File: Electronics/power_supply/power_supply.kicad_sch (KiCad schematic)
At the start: 83 parts, among them IC1 TLV76033DBZR, IC2 LM5069MMX-2_NOPB, J1 Conn_01x02_Male, J10 9801-0-15-15-23-27-10-0, J12 9801-0-15-15-23-27-10-0, J13 9801-0-15-15-23-27-10-0, J14 9801-0-15-15-23-27-10-0, J2 9801-0-15-15-23-27-10-0, J3 Conn_01x02_Male, J4 821-22-002-10-001101, J5 9801-0-15-15-23-27-10-0, J6 Conn_01x04_Male, J7 Conn_01x02_Male, J8 Conn_01x02_Male, J9 Conn_01x02_Pin, Q1 IPD90N04S4L04ATMA1, Q3 BC857, U1 R-78B5.0-2.0, U2 INA226, U3 INA226

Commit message: PCB fixup
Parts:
- added C30: 0.1uF 50V, Capacitor_SMD:C_0402_1005Metric_Pad0.74x0.62mm_HandSolder, symbol Device:C
- Q3: value BC857 -> MMBT5401; Mouser 583-C857 -> 165-8634
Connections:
- net at IC2.1 (SENSE), R8.1: now also C30.1
- net at IC2.2 (VIN), IC2.3 (UVLO), R8.4: now also C30.2
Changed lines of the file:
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@@
 	)
 	(junction
+		(at 158.75 219.71)
+		(diameter 0)
+		(color 0 0 0 0)
+	)
+	(junction
 		(at 254 246.38)
 		(diameter 0)
@@
 	)
 	(junction
+		(at 162.56 210.82)
+		(diameter 0)
+		(color 0 0 0 0)
+	)
+	(junction
 		(at 351.79 45.72)
 		(diameter 0)
@@
 	(wire
 		(pts
-			(xy 142.24 219.71) (xy 160.02 219.71)
+			(xy 142.24 219.71) (xy 158.75 219.71)
 		)
 		(stroke
@@
 	(wire
 		(pts
-			(xy 162.56 208.28) (xy 162.56 217.17)
+			(xy 162.56 208.28) (xy 162.56 210.82)
 		)
 		(stroke
@@
 	(wire
 		(pts
+			(xy 162.56 210.82) (xy 162.56 217.17)
+		)
+		(stroke
+			(width 0)
+			(type default)
+		)
+	)
+	(wire
+		(pts
 			(xy 341.63 203.2) (xy 346.71 203.2)
 		)
@@
 	(wire
 		(pts
+			(xy 158.75 219.71) (xy 160.02 219.71)
+		)
+		(stroke
+			(width 0)
+			(type default)
+		)
+	)
+	(wire
+		(pts
 			(xy 294.64 95.25) (xy 297.18 95.25)
 		)
@@
 	(wire
 		(pts
+			(xy 158.75 218.44) (xy 158.75 219.71)
+		)
+		(stroke
+			(width 0)
+			(type default)
+		)
+	)
+	(wire
+		(pts
 			(xy 327.66 87.63) (xy 327.66 85.09)
 		)
@@
 	(wire
 		(pts
+			(xy 158.75 210.82) (xy 162.56 210.82)
+		)
+		(stroke
+			(width 0)
+			(type default)
+		)
+	)
+	(wire
+		(pts
 			(xy 74.93 111.76) (xy 74.93 114.3)
 		)
@@
 	(symbol
 		(lib_id "Device:C")
+		(at 158.75 214.63 0)
+		(unit 1)
+		(exclude_from_sim no)
+		(in_bom yes)
+		(on_board yes)
+		(dnp yes)
+		(property "Reference" "C30"
+			(at 153.67 213.36 0)
+			(effects
+				(font
+					(size 1.016 1.016)
+				)
+				(justify left top)
+			)
+		)
+		(property "Value" "0.1uF 50V"
+			(at 153.67 218.44 0)
+			(effects
+				(font
+					(size 1.016 1.016)
+				)
+				(justify left bottom)
+			)
+		)
+		(property "Footprint" "Capacitor_SMD:C_0402_1005Metric_Pad0.74x0.62mm_HandSolder"
+			(at 159.7152 218.44 0)
+			(effects
+				(font
+					(size 1.27 1.27)
+				)
+				(hide yes)
+			)
+		)
+		(property "Datasheet" "~"
+			(at 158.75 214.63 0)
+			(effects
+				(font
+					(size 1.27 1.27)
+				)
+				(hide yes)
+			)
+		)
+		(property "Description" ""
+			(at 158.75 214.63 0)
+			(effects
+				(font
+					(size 1.27 1.27)
+				)
+				(hide yes)
+			)
+		)
+		(property "MF" "TDK"
+			(at 158.75 214.63 0)
+			(effects
+				(font
+					(size 1.27 1.27)
+				)
+				(justify left bottom)
+				(hide yes)
+			)
+		)
+		(property "MPN" "CGA2B3X7R1H104K050BB"
+			(at 158.75 214.63 0)
+			(effects
+				(font
+					(size 1.27 1.27)
+				)
+				(justify left bottom)
+				(hide yes)
+			)
+		)
+		(property "RS" "    247-7824"
+			(at 158.75 214.63 0)
+			(effects
+				(font
+					(size 1.27 1.27)
+				)
+				(hide yes)
+			)
+		)
+		(pin "1"
+		)
+		(pin "2"
+		)
+		(instances
+			(project "power_supply"
+				(path "/700fe2ea-26be-4d6c-908e-561c97acbca5"
+					(reference "C30")
+					(unit 1)
+				)
+			)
+		)
+	)
+	(symbol
+		(lib_id "Device:C")
 		(at 288.29 53.34 0)
 		(unit 1)
@@
 			)
 		)
-		(property "Value" "BC857"
+		(property "Value" "MMBT5401"
 			(at 251.46 255.2701 0)
 			(effects
@@
 			)
 		)
-		(property "Mouser" " 583-C857 "
+		(property "Mouser" "    165-8634"
 			(at 246.38 256.54 0)
 			(effects

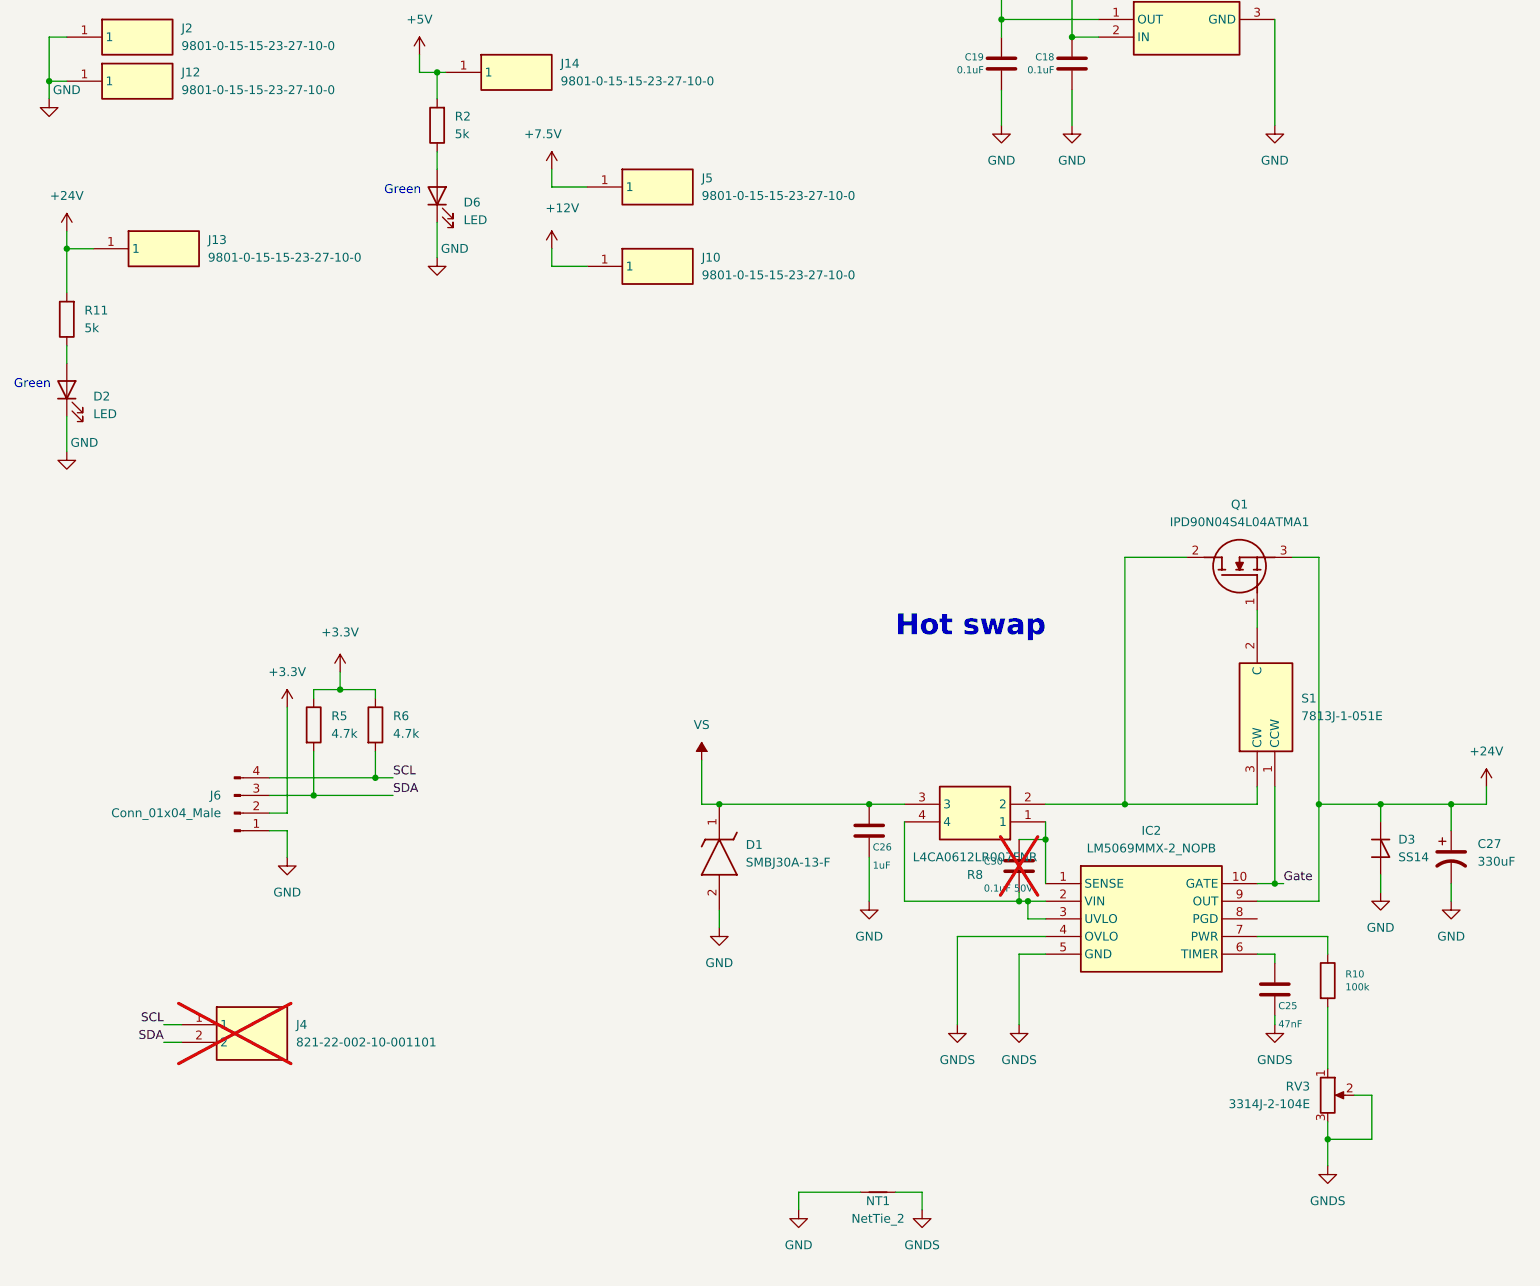
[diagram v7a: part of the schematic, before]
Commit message: Add main PCB for 2026
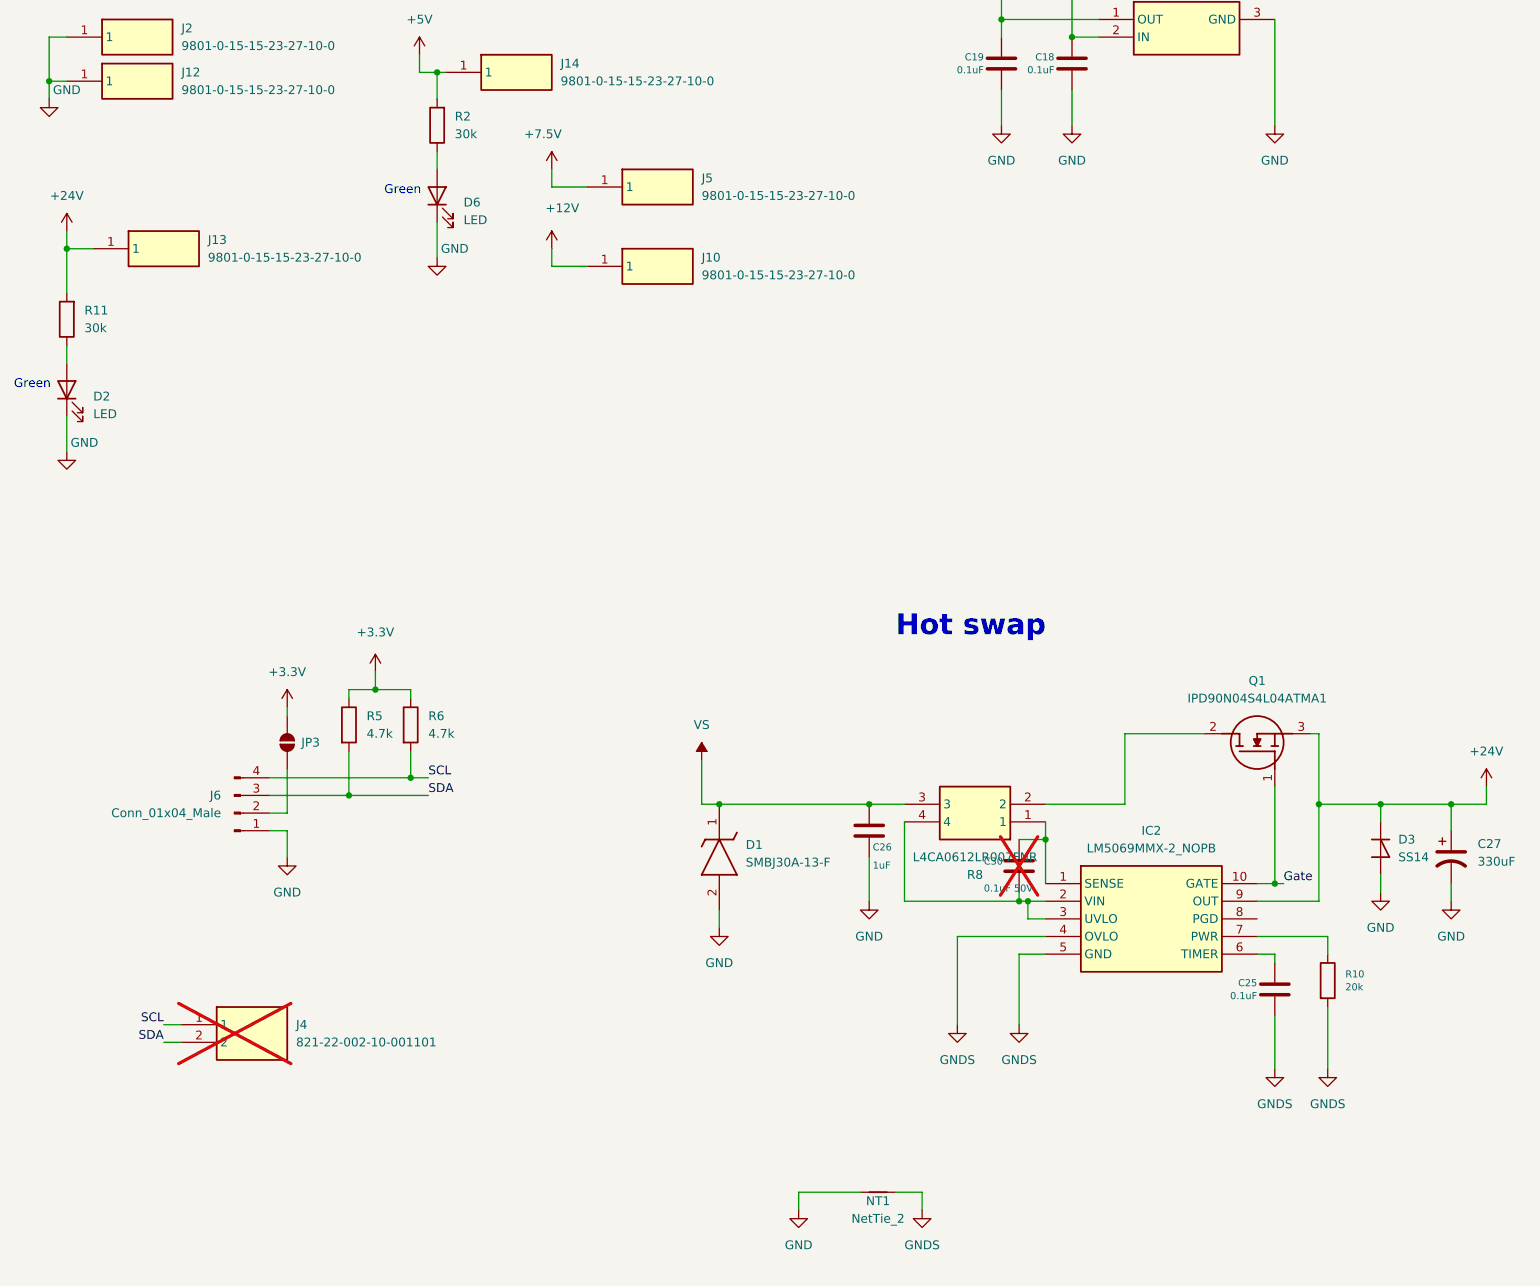
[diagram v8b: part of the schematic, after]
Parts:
- removed RV3: 3314J-2-104E, Potentiometer_SMD:Potentiometer_Bourns_3314J_Vertical, symbol Device:R_Potentiometer
- removed S1: 7813J-1-051E, MiAM:7813J1051E, symbol MiAM:7813J-1-051E
- added JP3: SolderJumper_2_Open, Jumper:SolderJumper-2_P1.3mm_Open_RoundedPad1.0x1.5mm, symbol Jumper:SolderJumper_2_Open
- C25: value 47nF -> 0.1uF; footprint Capacitor_SMD:C_0805_2012Metric_Pad1.18x1.45mm_HandSolder -> Capacitor_SMD:C_0805_2012Metric; MF TDK -> (none); MPN 0805YC473KAT2A -> (none); Mouser Part Number 581-0805YC473K -> (none)
- R10: value 100k -> 20k
- R11, R2: value 5k -> 30k
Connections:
- net +3.3V: now also JP3.2 (B); no longer J6.2 (Pin_2)
- net GNDS: now also R10.2
- net Gate: now also Q1.1 (G)
- new net: J6.2 (Pin_2), JP3.1 (A)
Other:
- moved on the sheet: Q1, R5, R6
